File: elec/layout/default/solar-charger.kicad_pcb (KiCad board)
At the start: 2 copper layers, 25 x 27.4 mm, 18 parts

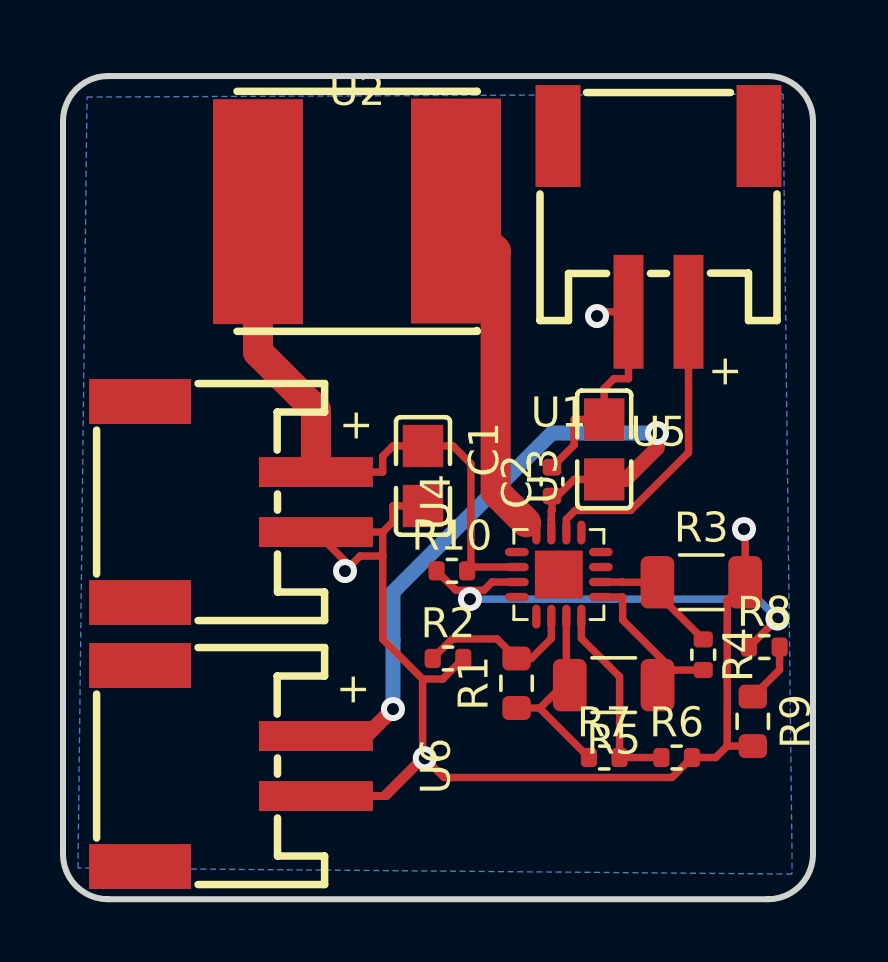
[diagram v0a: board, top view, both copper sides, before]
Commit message: solar charger fix gnd connections
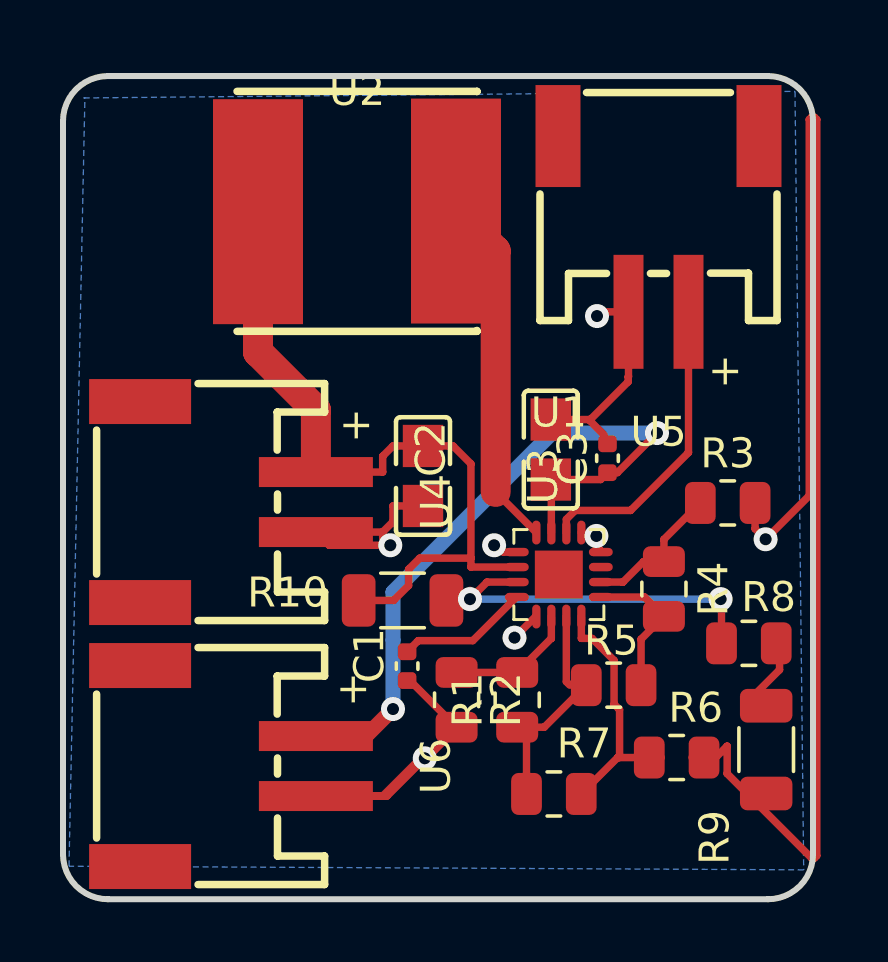
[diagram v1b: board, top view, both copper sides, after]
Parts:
- added C3: 16V 100nF X7R ±10% 0402 Multilayer Ceramic Capacitors MLCC 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, lib:C0402, F.Cu at (156.2, 50.7)
- C1: value Multilayer Ceramic Capacitors MLCC - SMD/SMT 4.7uF 16V 0805 RoHS -> 50V 10nF X7R ±10% 0402 Multilayer Ceramic Capacitors MLCC - SMD/SMT ROHS; footprint lib:C0805 -> lib:C0402
- C2: value Multilayer Ceramic Capacitors MLCC - SMD/SMT 100nF 10V 0402 RoHS -> 25V 4.7uF X5R ±10% 0805 Multilayer Ceramic Capacitors MLCC - SMD/SMT ROHS; footprint lib:C0402 -> lib:C0805
- R1: value 100mW Thick Film Resistors ±100ppm/℃ ±1% 5.1MΩ 0603 Chip Resistor - Surface Mount ROHS -> 125mW Thick Film Resistors 150V ±100ppm/℃ ±1% 5.1MΩ 0805 Chip Resistor - Surface Mount ROHS; footprint lib:R0603 -> lib:R0805
- R10: value 62.5mW Thick Film Resistors ±100ppm/℃ ±1% 4.02MΩ 0402 Chip Resistor - Surface Mount ROHS -> 250mW Thick Film Resistors 200V ±100ppm/℃ ±1% 4.02MΩ 1206 Chip Resistor - Surface Mount ROHS; footprint lib:R0402 -> lib:R1206
- R2: value 62.5mW Thick Film Resistors ±100ppm/℃ ±1% 4.87MΩ 0402 Chip Resistor - Surface Mount ROHS -> 125mW Thick Film Resistors 150V ±100ppm/℃ ±1% 4.87MΩ 0805 Chip Resistor - Surface Mount ROHS; footprint lib:R0402 -> lib:R0805
- R3: value 250mW Thick Film Resistors 200V ±100ppm/℃ ±1% -55℃~+155℃ 4.42MΩ 1206 Chip Resistor - Surface Mount ROHS -> 125mW Thick Film Resistors 150V ±100ppm/℃ ±1% 4.42MΩ 0805 Chip Resistor - Surface Mount ROHS; footprint lib:R1206 -> lib:R0805
- R4: value 62.5mW Thick Film Resistors ±100ppm/℃ ±1% 4.87MΩ 0402 Chip Resistor - Surface Mount ROHS -> 125mW Thick Film Resistors 150V ±100ppm/℃ ±1% 4.75MΩ 0805 Chip Resistor - Surface Mount ROHS; footprint lib:R0402 -> lib:R0805
- R5: value 250mW Thick Film Resistors ±100ppm/℃ ±1% 715kΩ 1206 Chip Resistor - Surface Mount ROHS -> 125mW Thick Film Resistors ±100ppm/℃ ±1% 715kΩ 0805 Chip Resistor - Surface Mount ROHS; footprint lib:R1206 -> lib:R0805
- R6, R7: value 62.5mW ±1% ±400ppm/℃ 4.99MΩ 0402 Chip Resistor - Surface Mount ROHS -> 125mW Thick Film Resistors ±100ppm/℃ ±1% 4.99MΩ 0805 Chip Resistor - Surface Mount ROHS; footprint lib:R0402 -> lib:R0805
- R8: value 62.5mW Thick Film Resistors ±100ppm/℃ ±1% 6.04MΩ 0402 Chip Resistor - Surface Mount ROHS -> 125mW Thick Film Resistors 150V ±100ppm/℃ ±1% 6.04MΩ 0805 Chip Resistor - Surface Mount ROHS; footprint lib:R0402 -> lib:R0805
- R9: value 100mW Thick Film Resistors ±100ppm/℃ ±1% 10MΩ 0603 Chip Resistor - Surface Mount ROHS -> 250mW Thick Film Resistors 200V ±100ppm/℃ ±1% 10MΩ 1206 Chip Resistor - Surface Mount ROHS; footprint lib:R0603 -> lib:R1206
- moved C1 9.77 mm to (149.5, 57.7), turned to -90 degrees
- moved R3 2.79 mm to (160.2, 52.2)
- moved R4 2.55 mm to (158.0, 55.1)
- moved R7 2.07 mm to (154.4, 61.9)
- moved R10 1.92 mm to (149.3, 55.5), turned to 180 degrees
- moved R2 1.41 mm to (151.1, 58.8), turned to -90 degrees
- moved C2 1.07 mm to (154.3, 50.5)
- moved R9 1.04 mm to (161.4, 60.5)
- moved R1 0.55 mm to (153.1, 58.8)
- moved R8 0.53 mm to (160.9, 56.9)
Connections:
- net _3 renamed sol_jst_conn-_3
- net _3-1 renamed bat_jst_conn-_3
- net _3-2 renamed load_jst_conn-_3
- net _4 renamed sol_jst_conn-_4
- net _4-1 renamed bat_jst_conn-_4
- net _4-2 renamed load_jst_conn-_4
- C1 pad 1: vcc -> vref_samp
- U1 pad 1: vss -> gnd
- U1 pad 12: avss -> gnd
- U1 pad 13: vss2 -> gnd
- U1 pad 5: ot_prog -> gnd
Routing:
- net gnd: track 52.8 -> 77.3 mm, vias 4 -> 7
- net _1: track 20.7 -> 25.2 mm
- net vref_samp: track 0.00 -> 4.41 mm
- net voc_samp: track 15.2 -> 12.8 mm
- net vbat_uv: track 6.62 -> 8.61 mm
- net vbat_ov: track 5.50 -> 3.78 mm
- net vrdiv: track 6.68 -> 8.01 mm
- net ok_hyst: track 5.58 -> 4.98 mm
